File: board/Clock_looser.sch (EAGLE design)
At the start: 17 parts

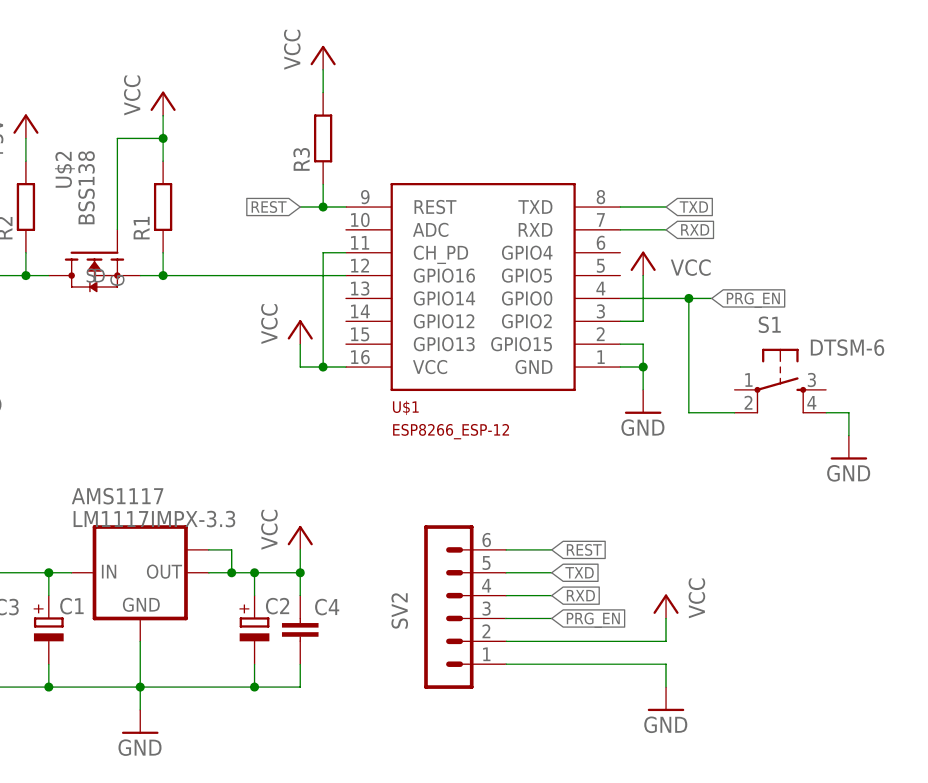
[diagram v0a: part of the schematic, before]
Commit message: Added LEDs and a photoresistor
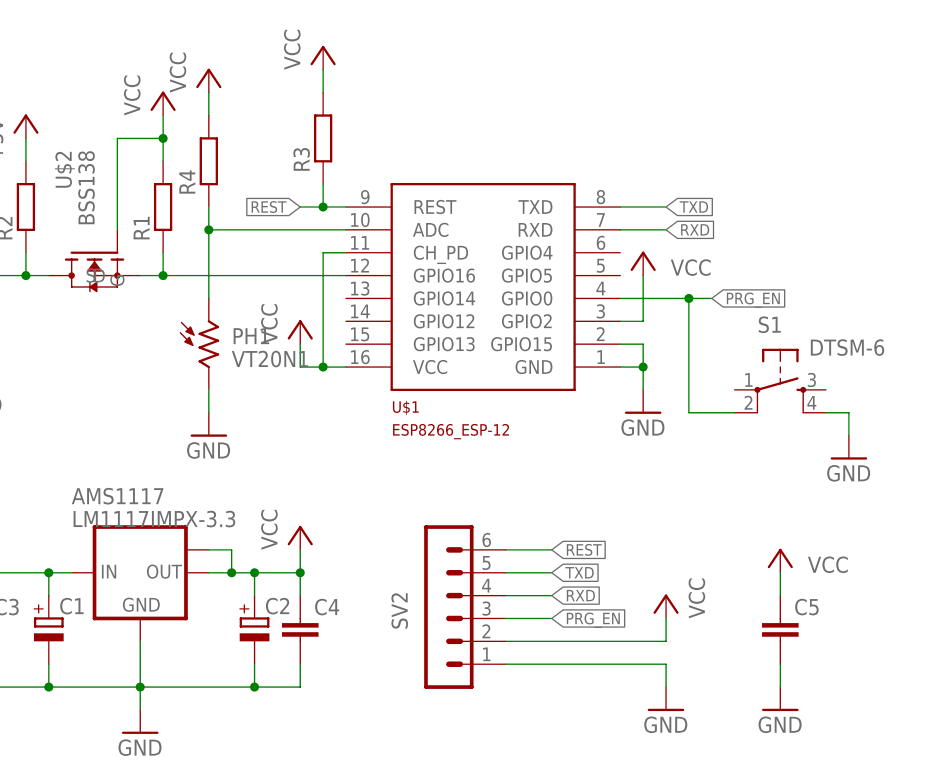
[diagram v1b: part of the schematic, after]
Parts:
- added C5: (no value), rcl:C-EUC0805
- added PH1: VT20N1, photo-elements:VT20N1
- added R4: (no value), rcl:R-EU_R0805
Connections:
- new net ADC: PH1.1, R4.1, U$1.ADC
- net GND: now also C5.2, PH1.2
- net VCC: now also C5.1, R4.2
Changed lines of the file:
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@@
 <layers>
 <layer number="1" name="Top" color="4" fill="1" visible="yes" active="no"/>
+<layer number="2" name="Route2" color="1" fill="3" visible="yes" active="no"/>
+<layer number="3" name="Route3" color="4" fill="3" visible="yes" active="no"/>
+<layer number="4" name="Route4" color="1" fill="4" visible="yes" active="no"/>
+<layer number="5" name="Route5" color="4" fill="4" visible="yes" active="no"/>
+<layer number="6" name="Route6" color="1" fill="8" visible="yes" active="no"/>
+<layer number="7" name="Route7" color="4" fill="8" visible="yes" active="no"/>
+<layer number="8" name="Route8" color="1" fill="2" visible="yes" active="no"/>
+<layer number="9" name="Route9" color="4" fill="2" visible="yes" active="no"/>
+<layer number="10" name="Route10" color="1" fill="7" visible="yes" active="no"/>
+<layer number="11" name="Route11" color="4" fill="7" visible="yes" active="no"/>
+<layer number="12" name="Route12" color="1" fill="5" visible="yes" active="no"/>
+<layer number="13" name="Route13" color="4" fill="5" visible="yes" active="no"/>
+<layer number="14" name="Route14" color="1" fill="6" visible="yes" active="no"/>
+<layer number="15" name="Route15" color="4" fill="6" visible="yes" active="no"/>
 <layer number="16" name="Bottom" color="1" fill="1" visible="yes" active="no"/>
 <layer number="17" name="Pads" color="2" fill="1" visible="yes" active="no"/>
@@
 <part name="P+11" library="supply1" library_urn="urn:adsk.eagle:library:371" deviceset="+5V" device=""/>
 <part name="P+12" library="supply1" library_urn="urn:adsk.eagle:library:371" deviceset="+5V" device=""/>
+<part name="C5" library="rcl" library_urn="urn:adsk.eagle:library:334" deviceset="C-EU" device="C0805"/>
+<part name="P+13" library="supply1" library_urn="urn:adsk.eagle:library:371" deviceset="VCC" device=""/>
+<part name="GND9" library="supply1" library_urn="urn:adsk.eagle:library:371" deviceset="GND" device=""/>
+<part name="PH1" library="photo-elements" library_urn="urn:adsk.eagle:library:323" deviceset="VT2*" device="" technology="0N1"/>
+<part name="R4" library="rcl" library_urn="urn:adsk.eagle:library:334" deviceset="R-EU_" device="R0805"/>
+<part name="P+14" library="supply1" library_urn="urn:adsk.eagle:library:371" deviceset="VCC" device=""/>
+<part name="GND10" library="supply1" library_urn="urn:adsk.eagle:library:371" deviceset="GND" device=""/>
 </parts>
 <sheets>
@@
 <instance part="P+11" gate="1" x="-40.64" y="55.88"/>
 <instance part="P+12" gate="1" x="-73.66" y="55.88"/>
+<instance part="C5" gate="G$1" x="48.26" y="5.08"/>
+<instance part="P+13" gate="VCC" x="48.26" y="12.7" smashed="yes" rot="MR0">
+<attribute name="VALUE" x="55.88" y="10.16" size="1.778" layer="96" rot="MR0"/>
+</instance>
+<instance part="GND9" gate="1" x="48.26" y="-5.08"/>
+<instance part="PH1" gate="G$1" x="-15.24" y="35.56"/>
+<instance part="R4" gate="G$1" x="-15.24" y="55.88" rot="R90"/>
+<instance part="P+14" gate="VCC" x="-15.24" y="66.04"/>
+<instance part="GND10" gate="1" x="-15.24" y="25.4"/>
 </instances>
 <busses>
@@
 <wire x1="-40.64" y1="35.56" x2="-40.64" y2="33.02" width="0.1524" layer="91"/>
 </segment>
+<segment>
+<pinref part="C5" gate="G$1" pin="2"/>
+<pinref part="GND9" gate="1" pin="GND"/>
+<wire x1="48.26" y1="-2.54" x2="48.26" y2="0" width="0.1524" layer="91"/>
+</segment>
+<segment>
+<pinref part="PH1" gate="G$1" pin="2"/>
+<pinref part="GND10" gate="1" pin="GND"/>
+<wire x1="-15.24" y1="27.94" x2="-15.24" y2="30.48" width="0.1524" layer="91"/>
+</segment>
 </net>
 <net name="N$9" class="0">
@@
 <wire x1="35.56" y1="5.08" x2="35.56" y2="2.54" width="0.1524" layer="91"/>
 </segment>
+<segment>
+<pinref part="C5" gate="G$1" pin="1"/>
+<pinref part="P+13" gate="VCC" pin="VCC"/>
+<wire x1="48.26" y1="10.16" x2="48.26" y2="7.62" width="0.1524" layer="91"/>
+</segment>
+<segment>
+<pinref part="R4" gate="G$1" pin="2"/>
+<pinref part="P+14" gate="VCC" pin="VCC"/>
+<wire x1="-15.24" y1="63.5" x2="-15.24" y2="60.96" width="0.1524" layer="91"/>
+</segment>
 </net>
 <net name="N$7" class="0">
@@
 </segment>
 </net>
+<net name="ADC" class="0">
+<segment>
+<pinref part="U$1" gate="G$1" pin="ADC"/>
+<pinref part="R4" gate="G$1" pin="1"/>
+<wire x1="0" y1="48.26" x2="-15.24" y2="48.26" width="0.1524" layer="91"/>
+<wire x1="-15.24" y1="48.26" x2="-15.24" y2="50.8" width="0.1524" layer="91"/>
+<pinref part="PH1" gate="G$1" pin="1"/>
+<wire x1="-15.24" y1="40.64" x2="-15.24" y2="48.26" width="0.1524" layer="91"/>
+<junction x="-15.24" y="48.26"/>
+</segment>
+</net>

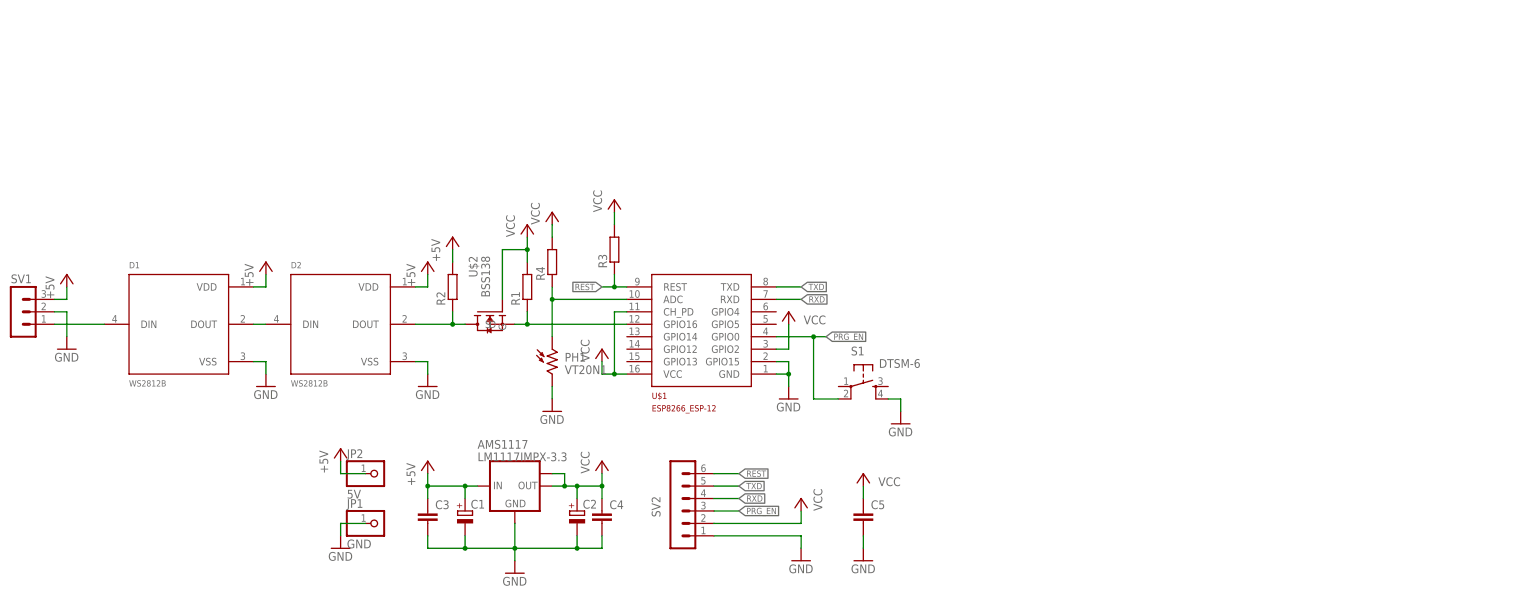
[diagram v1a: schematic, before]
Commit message: Improved clearance
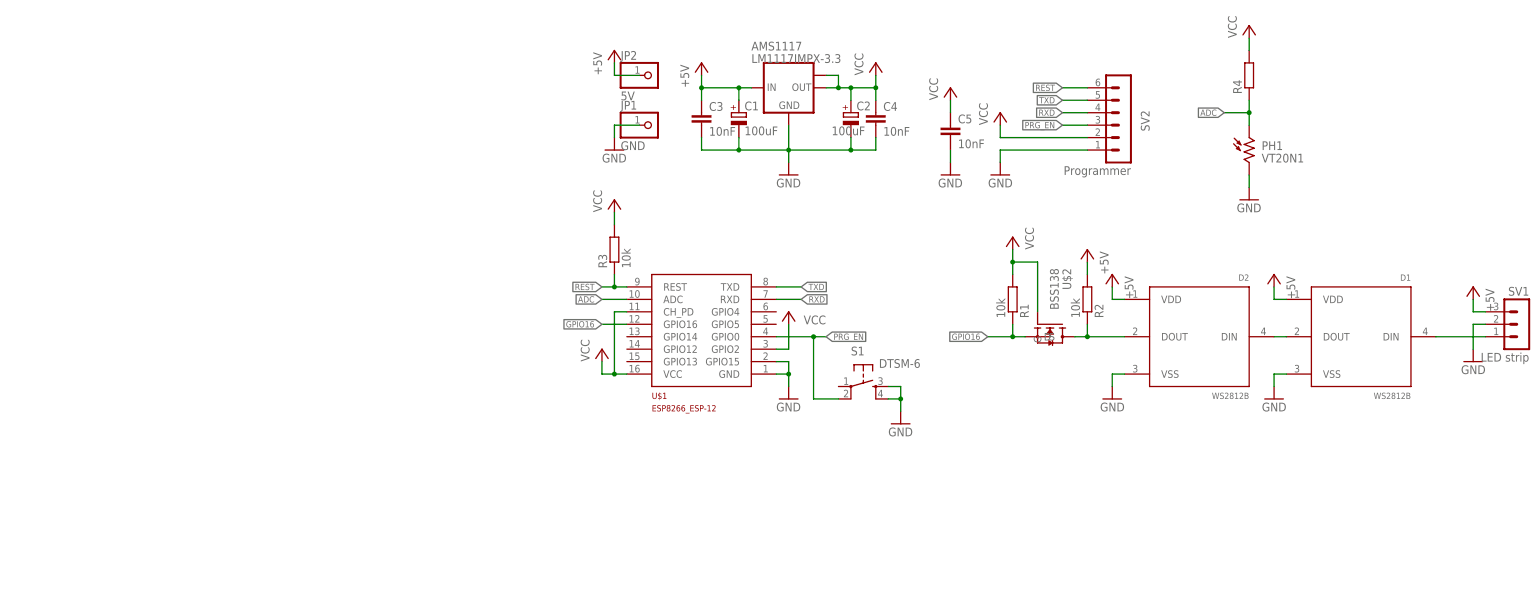
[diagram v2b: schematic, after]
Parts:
- C1, C2: value (none) -> 100uF
- C3, C4, C5: value (none) -> 10nF
- R1, R2, R3: value (none) -> 10k
- SV1: value (none) -> LED strip
- SV2: value (none) -> Programmer
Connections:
- net N$9 renamed GPIO16
- net GND: now also S1.3
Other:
- moved on the sheet: AMS1117, C1, C2, C3, C4, C5, D1, D2, JP1, JP2, PH1, R1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
